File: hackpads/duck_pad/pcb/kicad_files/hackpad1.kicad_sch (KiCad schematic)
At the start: 40 parts, among them U2 MCU_Seeed_XIAO_RP2040

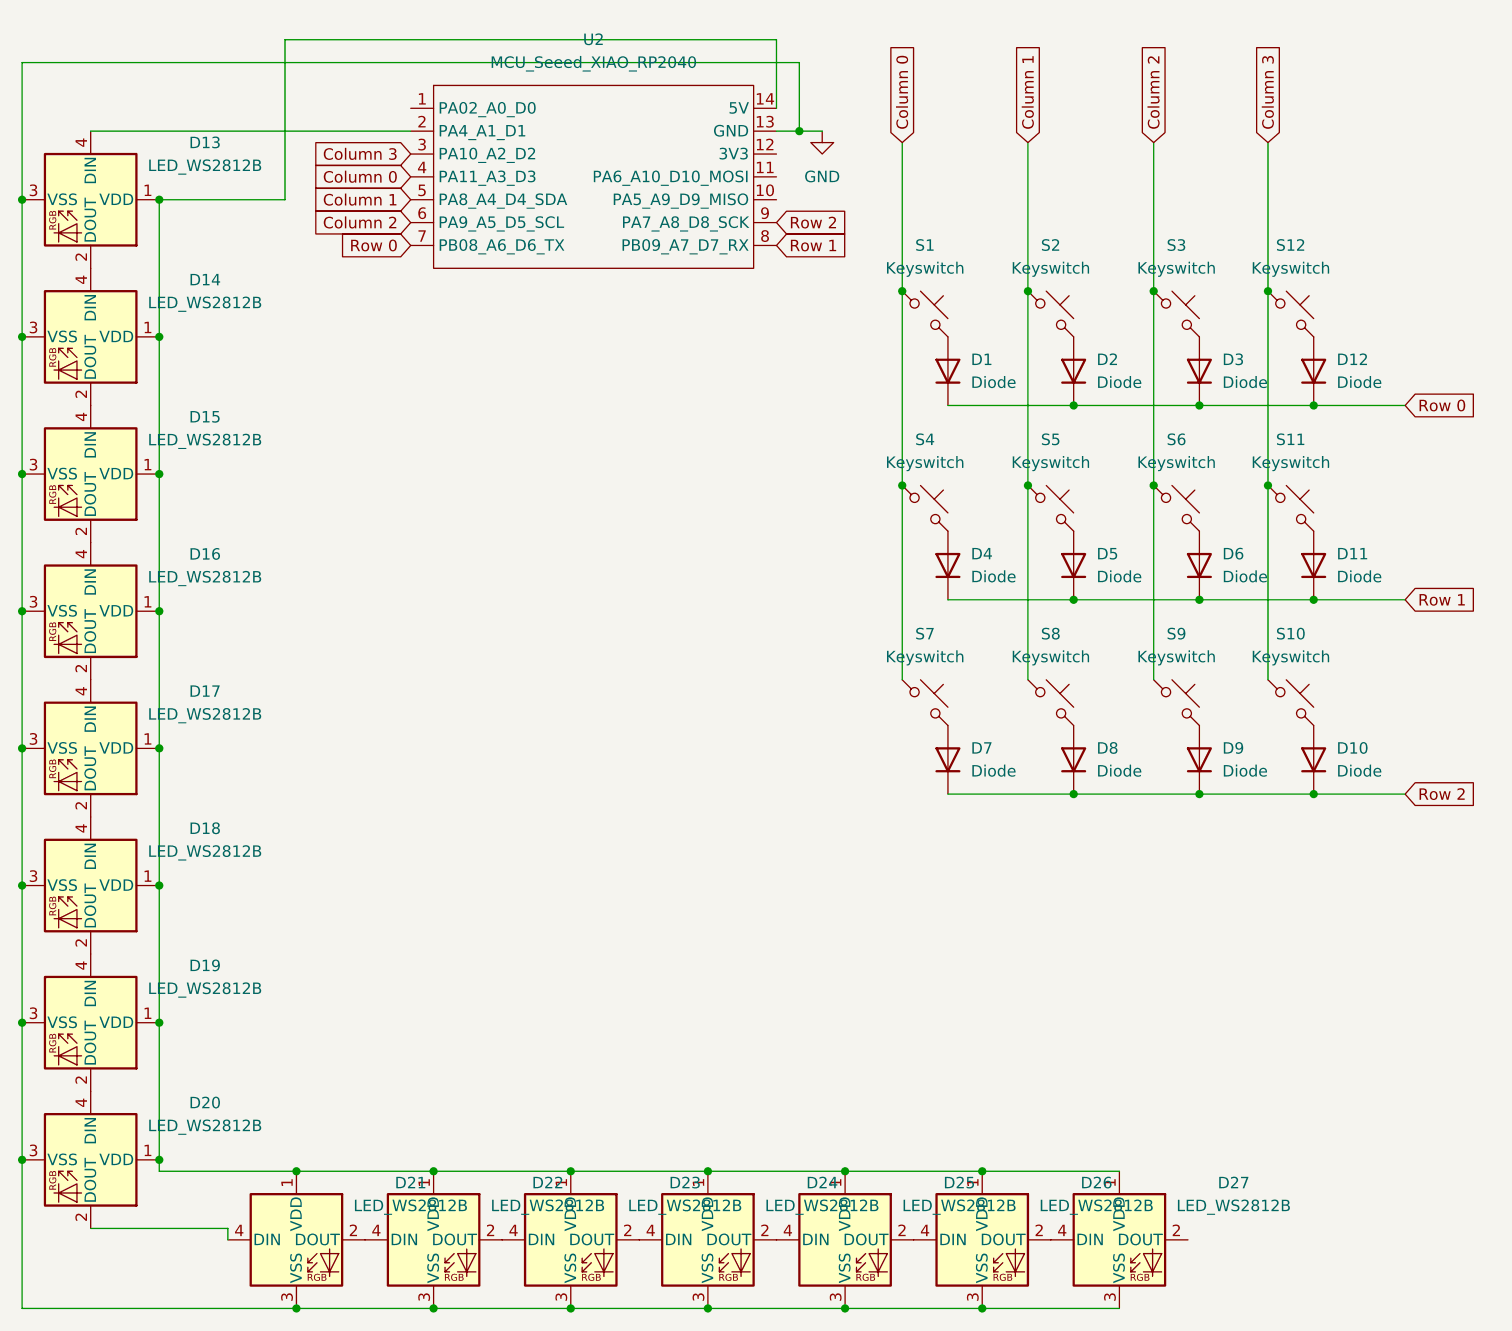
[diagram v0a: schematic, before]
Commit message: SMDs removed
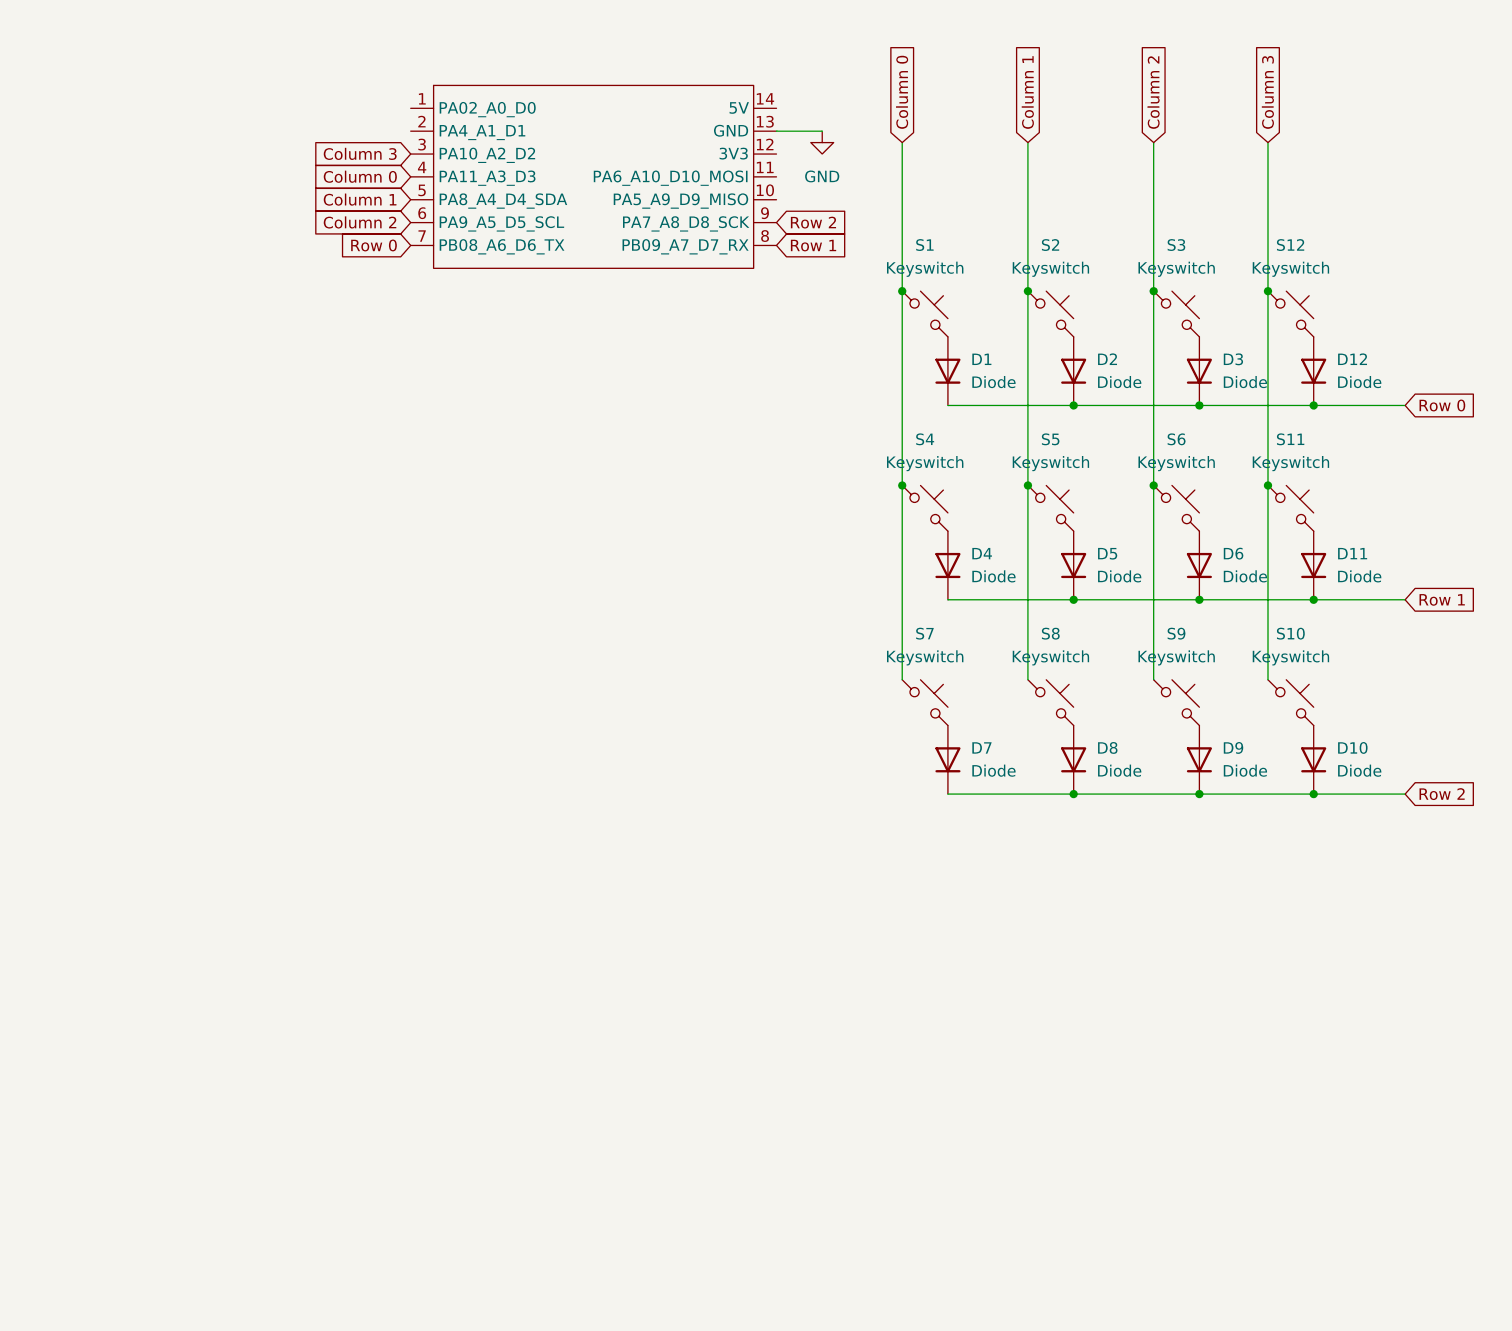
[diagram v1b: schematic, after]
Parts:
- removed D13, D14, D15, D16, D17, D18, D19, D20, D21, D22, D23, D24, D25, D26, D27: LED_WS2812B, ScottoKeebs_Components:LED_WS2812B, symbol ScottoKeebs:LED_WS2812B
